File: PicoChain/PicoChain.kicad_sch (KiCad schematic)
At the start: 14 parts, among them J1 RJ45, J2 RJ45, J3 Conn_01x02_Socket, J4 Conn_01x02_Socket, J5 Conn_01x20_Socket, J6 Conn_01x20_Socket, U1 PCA9615DP, U2 RASPBERRY_PI_PICO

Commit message: Updated to version 1.1
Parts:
- removed R1, R3, R4, R6: 470, Resistor_SMD:R_0805_2012Metric, symbol Device:R
- removed R2, R5: 140, Resistor_SMD:R_0805_2012Metric, symbol Device:R
- added C1, C2, C3, C4: 330nF, Capacitor_Tantalum_SMD:CP_EIA-3216-18_Kemet-A, symbol Device:C_Polarized
- added C5, C6: 10uF, Capacitor_Tantalum_SMD:CP_EIA-3528-21_Kemet-B, symbol Device:C_Polarized
- added U3, U4: LM78M05_TO252, Package_TO_SOT_SMD:TO-252-2, symbol Regulator_Linear:LM78M05_TO252
- added U5: LM1085-12, LM1085IS-12:TO254P1524X483-4N, symbol Regulator_Linear:LM1085-12
- U2: footprint MCU_RaspberryPi_and_Boards:RPi_Pico_SMD_TH -> RASPBERRY_PI_PICO:RASPBERRY_PI_PICO
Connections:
- net +12V: now also J1.8, J2.8, C1.1, C3.1, U3.1 (VI), U4.1 (VI); no longer J1.6, J2.6, J3.1 (Pin_1)
- net +5V: now also C2.1, U3.3 (VO); no longer J1.3, J2.3
- net +5V(M): now also C4.1, U4.3 (VO); no longer J1.5, J2.5
- net GND: now also J1.1, J1.7, J2.1, J2.7, C1.2, C2.2, C3.2, C4.2, C5.2, C6.2, U3.2 (GND), U4.2 (GND), U5.1 (GND); no longer J1.4, J2.4
- net +24V: now reaches J1.2, J2.2
- net +24V: now also C5.1, U5.3 (VI); no longer U1.7 (DSCLP)
- new net: J1.3, J2.3, U1.6 (DSCLM)
- new net: J1.4, J2.4, U1.7 (DSCLP)
- new net: J1.5, J2.5, U1.8 (DSDAP)
- new net: J1.6, J2.6, U1.9 (DSDAM)
- new net +12V(R): C6.1, J3.1 (Pin_1), U5.2 (VO)
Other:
- moved on the sheet: J3, J4, J5, J6, U1, U2

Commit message: Added licences and PDF schematics
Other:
- title: (none) -> PicoChain Reference Device Implementation
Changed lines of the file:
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@@
 	(generator_version "8.0")
 	(paper "A4")
+	(title_block
+		(title "PicoChain Reference Device Implementation")
+		(date "2024-08-22")
+		(rev "v1.1")
+		(comment 2 "http://www.tapr.org/OHL")
+		(comment 3 "Licence: The TAPR Open Hardware License")
+		(comment 4 "Author: Jason Alexander")
+	)
 	(junction
 		(at 86.36 82.55)

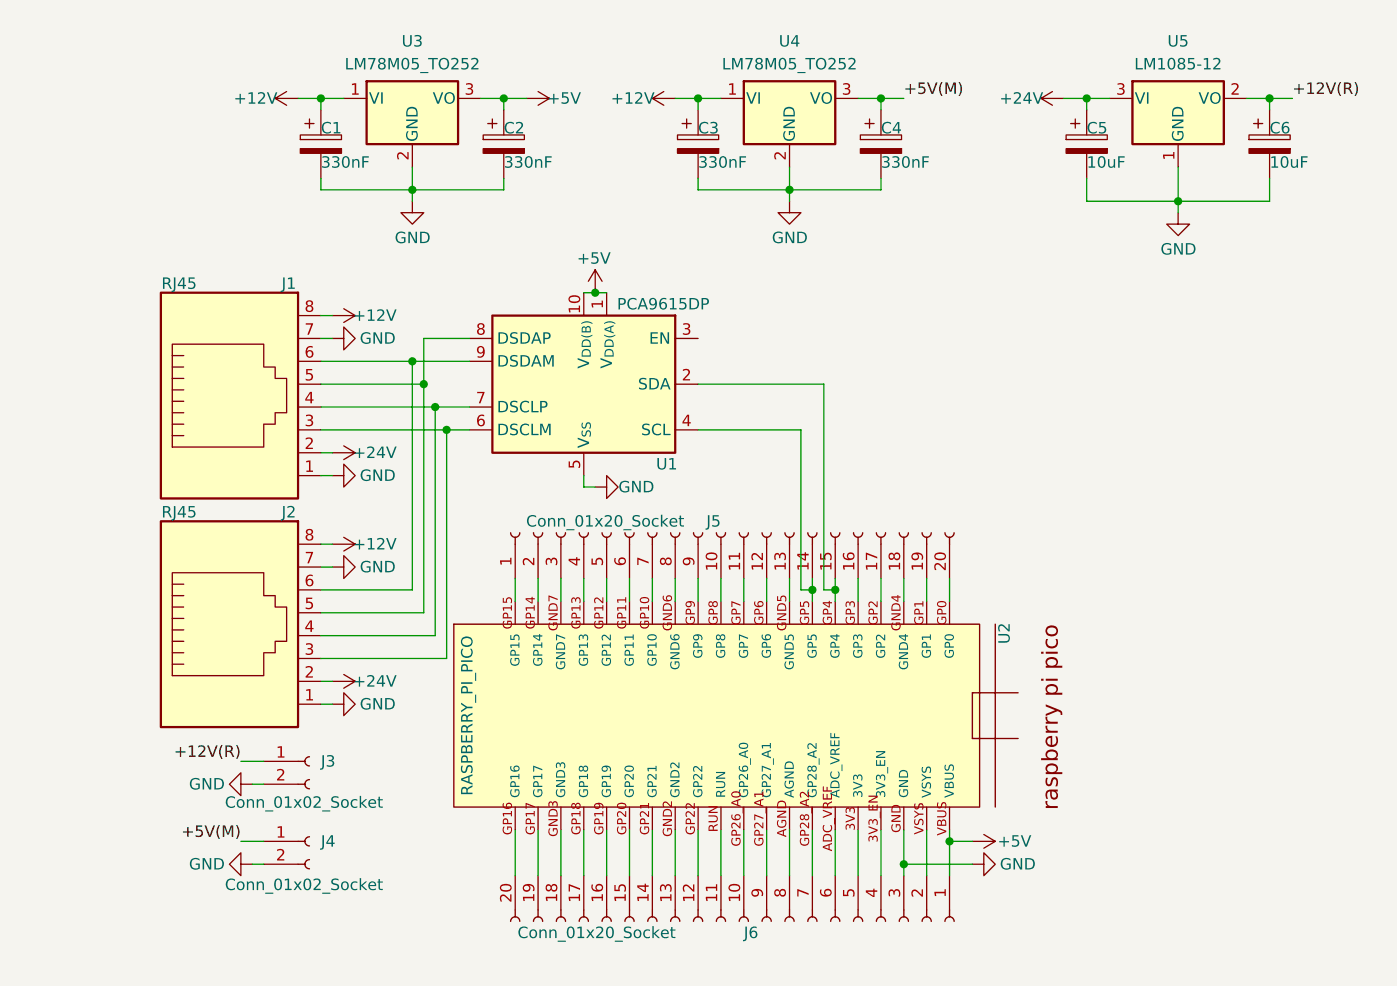
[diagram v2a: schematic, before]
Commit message: Updated PicoChainZero base board.
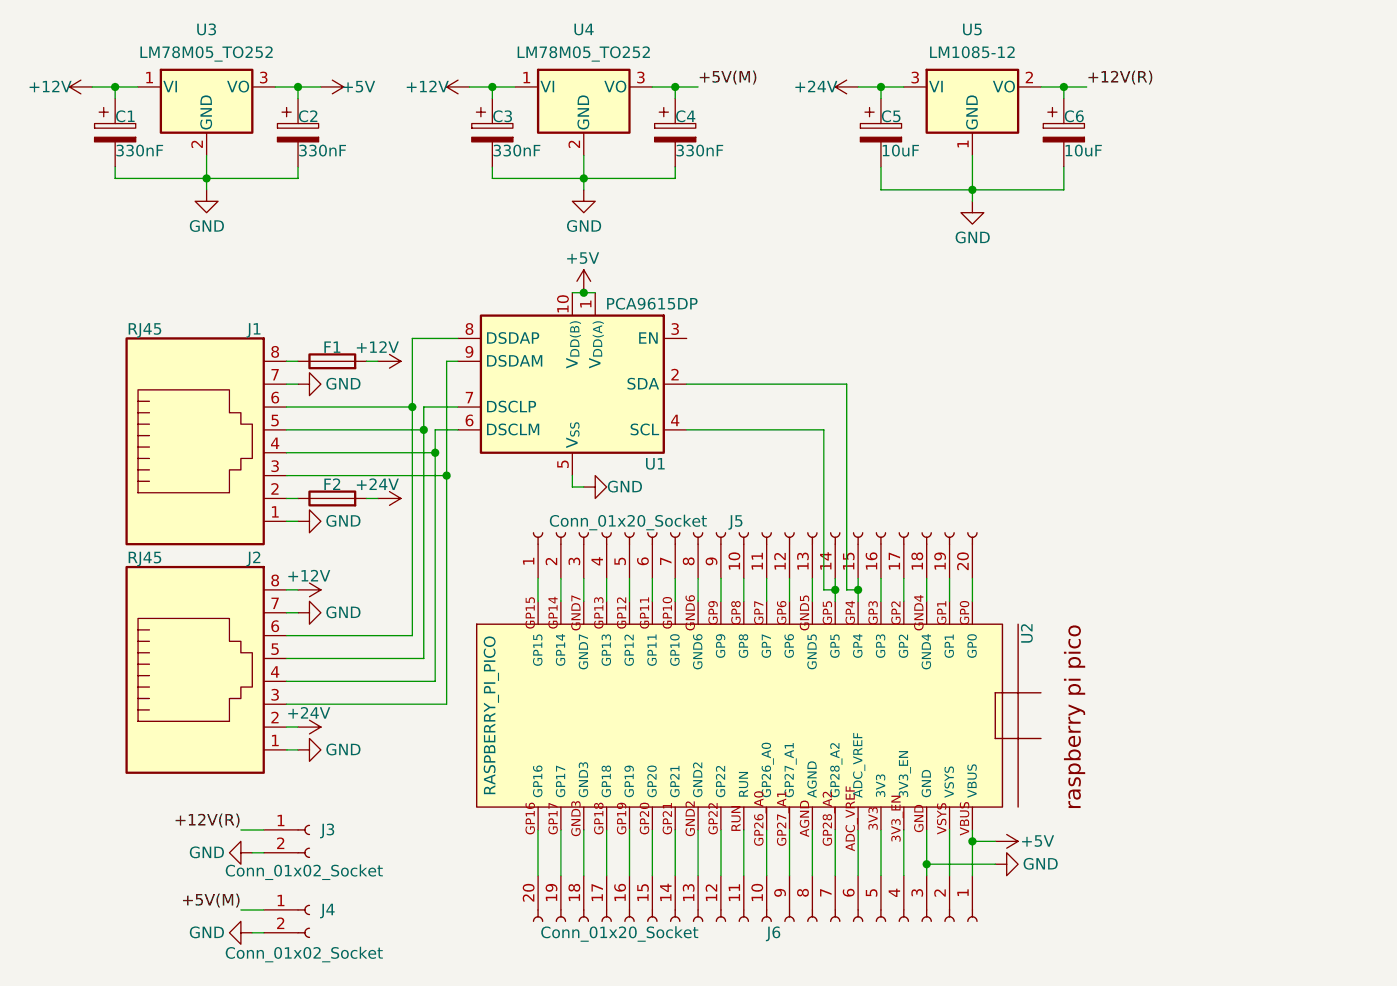
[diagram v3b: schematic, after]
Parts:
- added F1, F2: Fuse, Fuse:Fuse_0805_2012Metric, symbol Device:Fuse
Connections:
- net +12V: now also F1.2; no longer J1.8
- net +24V: now also F2.2; no longer J1.2
- net at J1.3, J2.3: now also U1.9 (DSDAM); no longer U1.6 (DSCLM)
- net at J1.4, J2.4: now also U1.6 (DSCLM); no longer U1.7 (DSCLP)
- net at J1.5, J2.5: now also U1.7 (DSCLP); no longer U1.8 (DSDAP)
- net at J1.6, J2.6: now also U1.8 (DSDAP); no longer U1.9 (DSDAM)
- new net: F2.1, J1.2
- new net: F1.1, J1.8
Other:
- moved on the sheet: C1, C2, C3, C4, C5, C6, J3, J4, J5, J6, U2, U3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
